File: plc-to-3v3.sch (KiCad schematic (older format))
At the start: 12 parts, among them Q10 2N7002, Q11 2N7002, Q12 2N7002

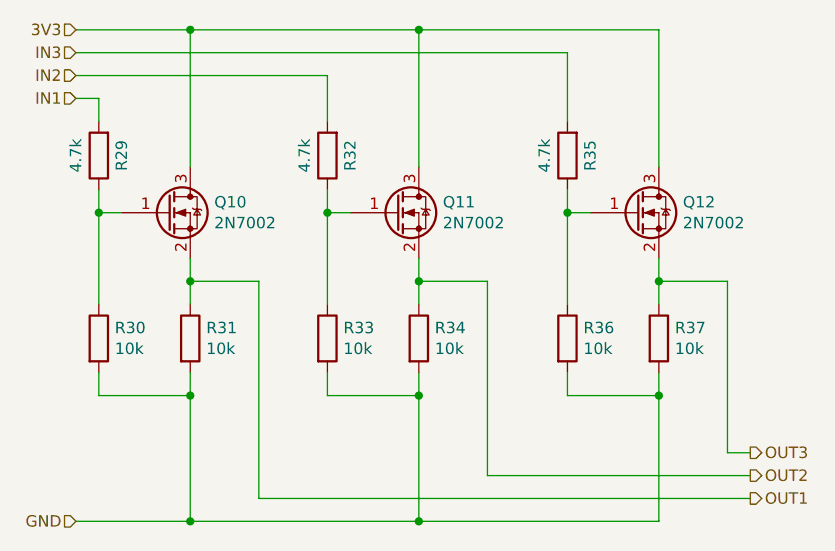
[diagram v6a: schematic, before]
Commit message: Added mounting holes for M3 screws. Performed DRC check.
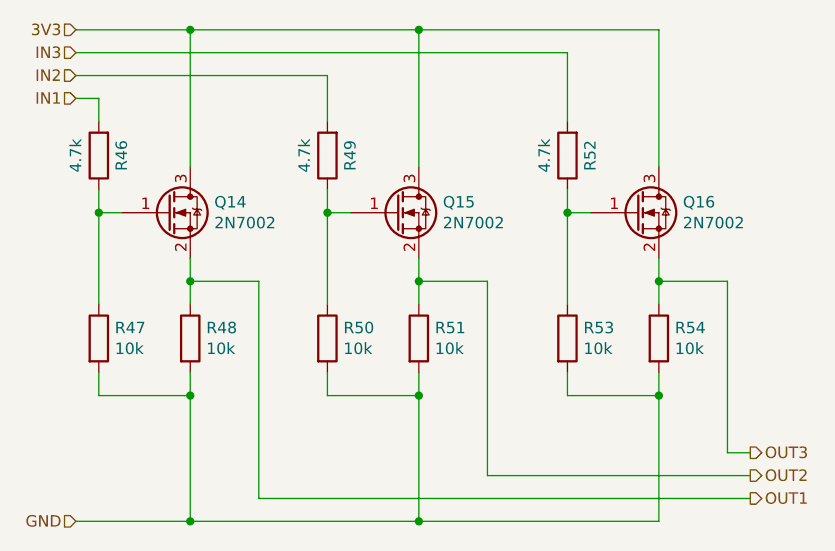
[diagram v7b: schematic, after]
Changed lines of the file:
@@
 AR Path="/5BF2FCD2/5BE6F709" Ref="R?"  Part="1"
 AR Path="/5C015BEE/5BE6F709" Ref="R54"  Part="1"
-F 0 "R37" H 7020 3946 50  0000 L CNN
+F 0 "R54" H 7020 3946 50  0000 L CNN
 F 1 "10k" H 7020 3855 50  0000 L CNN
 F 2 "Resistor_SMD:R_0603_1608Metric" V 6880 3900 50  0001 C CNN
@@
 AR Path="/5BF2FCD2/5BE6F700" Ref="R?"  Part="1"
 AR Path="/5C015BEE/5BE6F700" Ref="R53"  Part="1"
-F 0 "R36" H 6620 3946 50  0000 L CNN
+F 0 "R53" H 6620 3946 50  0000 L CNN
 F 1 "10k" H 6620 3855 50  0000 L CNN
 F 2 "Resistor_SMD:R_0603_1608Metric" V 6480 3900 50  0001 C CNN
@@
 AR Path="/5BF2FCD2/5BE6F6F8" Ref="R?"  Part="1"
 AR Path="/5C015BEE/5BE6F6F8" Ref="R52"  Part="1"
-F 0 "R35" V 6450 3100 50  0000 C CNN
+F 0 "R52" V 6450 3100 50  0000 C CNN
 F 1 "4.7k" V 6650 3100 50  0000 C CNN
 F 2 "Resistor_SMD:R_0603_1608Metric" V 6480 3100 50  0001 C CNN
@@
 AR Path="/5BF2FCD2/5BE6F6F1" Ref="Q?"  Part="1"
 AR Path="/5C015BEE/5BE6F6F1" Ref="Q16"  Part="1"
-F 0 "Q12" H 7055 3396 50  0000 L CNN
+F 0 "Q16" H 7055 3396 50  0000 L CNN
 F 1 "2N7002" H 7055 3305 50  0000 L CNN
 F 2 "Package_TO_SOT_SMD:SOT-23" H 7050 3275 50  0001 L CIN
@@
 AR Path="/5BF2FCD2/5BE6F6DA" Ref="R?"  Part="1"
 AR Path="/5C015BEE/5BE6F6DA" Ref="R51"  Part="1"
-F 0 "R34" H 5970 3946 50  0000 L CNN
+F 0 "R51" H 5970 3946 50  0000 L CNN
 F 1 "10k" H 5970 3855 50  0000 L CNN
 F 2 "Resistor_SMD:R_0603_1608Metric" V 5830 3900 50  0001 C CNN
@@
 AR Path="/5BF2FCD2/5BE6F6D2" Ref="R?"  Part="1"
 AR Path="/5C015BEE/5BE6F6D2" Ref="R50"  Part="1"
-F 0 "R33" H 5570 3946 50  0000 L CNN
+F 0 "R50" H 5570 3946 50  0000 L CNN
 F 1 "10k" H 5570 3855 50  0000 L CNN
 F 2 "Resistor_SMD:R_0603_1608Metric" V 5430 3900 50  0001 C CNN
@@
 AR Path="/5BF2FCD2/5BE6F6CA" Ref="R?"  Part="1"
 AR Path="/5C015BEE/5BE6F6CA" Ref="R49"  Part="1"
-F 0 "R32" V 5400 3100 50  0000 C CNN
+F 0 "R49" V 5400 3100 50  0000 C CNN
 F 1 "4.7k" V 5600 3100 50  0000 C CNN
 F 2 "Resistor_SMD:R_0603_1608Metric" V 5430 3100 50  0001 C CNN
@@
 AR Path="/5BF2FCD2/5BE6F6C3" Ref="Q?"  Part="1"
 AR Path="/5C015BEE/5BE6F6C3" Ref="Q15"  Part="1"
-F 0 "Q11" H 6005 3396 50  0000 L CNN
+F 0 "Q15" H 6005 3396 50  0000 L CNN
 F 1 "2N7002" H 6005 3305 50  0000 L CNN
 F 2 "Package_TO_SOT_SMD:SOT-23" H 6000 3275 50  0001 L CIN
@@
 AR Path="/5BF2FCD2/5BE6F6A5" Ref="R?"  Part="1"
 AR Path="/5C015BEE/5BE6F6A5" Ref="R48"  Part="1"
-F 0 "R31" H 4970 3946 50  0000 L CNN
+F 0 "R48" H 4970 3946 50  0000 L CNN
 F 1 "10k" H 4970 3855 50  0000 L CNN
 F 2 "Resistor_SMD:R_0603_1608Metric" V 4830 3900 50  0001 C CNN
@@
 AR Path="/5BF2FCD2/5BE6F69D" Ref="R?"  Part="1"
 AR Path="/5C015BEE/5BE6F69D" Ref="R47"  Part="1"
-F 0 "R30" H 4570 3946 50  0000 L CNN
+F 0 "R47" H 4570 3946 50  0000 L CNN
 F 1 "10k" H 4570 3855 50  0000 L CNN
 F 2 "Resistor_SMD:R_0603_1608Metric" V 4430 3900 50  0001 C CNN
@@
 AR Path="/5BF2FCD2/5BE6F695" Ref="R?"  Part="1"
 AR Path="/5C015BEE/5BE6F695" Ref="R46"  Part="1"
-F 0 "R29" V 4400 3100 50  0000 C CNN
+F 0 "R46" V 4400 3100 50  0000 C CNN
 F 1 "4.7k" V 4600 3100 50  0000 C CNN
 F 2 "Resistor_SMD:R_0603_1608Metric" V 4430 3100 50  0001 C CNN
@@
 AR Path="/5BF2FCD2/5BE6F68E" Ref="Q?"  Part="1"
 AR Path="/5C015BEE/5BE6F68E" Ref="Q14"  Part="1"
-F 0 "Q10" H 5005 3396 50  0000 L CNN
+F 0 "Q14" H 5005 3396 50  0000 L CNN
 F 1 "2N7002" H 5005 3305 50  0000 L CNN
 F 2 "Package_TO_SOT_SMD:SOT-23" H 5000 3275 50  0001 L CIN
